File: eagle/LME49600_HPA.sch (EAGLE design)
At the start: 41 parts, among them IC1 OPA2134P, IC2 OPA2134P

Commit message: Update: Eagle files
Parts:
- C18, C19, C6, C7: value 4.7uF -> 10uF
- R11, R2, R3, R6, R7, R8: value 1.2k -> 1k
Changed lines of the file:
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@@
 <part name="AGND1" library="supply1" deviceset="AGND" device=""/>
 <part name="IC1" library="burr-brown" deviceset="OPA2134" device="P"/>
-<part name="R2" library="rcl" deviceset="R-EU_" device="0207/7" value="1.2k"/>
+<part name="R2" library="rcl" deviceset="R-EU_" device="0207/7" value="1k"/>
 <part name="AGND3" library="supply1" deviceset="AGND" device=""/>
 <part name="C2" library="rcl" deviceset="C-EU" device="025-024X044" value="0.1uF"/>
@@
 <part name="AGND4" library="supply1" deviceset="AGND" device=""/>
 <part name="AGND5" library="supply1" deviceset="AGND" device=""/>
-<part name="R3" library="rcl" deviceset="R-EU_" device="0207/7" value="1.2k"/>
+<part name="R3" library="rcl" deviceset="R-EU_" device="0207/7" value="1k"/>
 <part name="P+1" library="supply1" deviceset="V+" device=""/>
 <part name="P-1" library="supply1" deviceset="V-" device=""/>
@@
 <part name="AGND8" library="supply1" deviceset="AGND" device=""/>
 <part name="AGND9" library="supply1" deviceset="AGND" device=""/>
-<part name="R6" library="rcl" deviceset="R-EU_" device="0207/7" value="1.2k"/>
+<part name="R6" library="rcl" deviceset="R-EU_" device="0207/7" value="1k"/>
 <part name="AGND11" library="supply1" deviceset="AGND" device=""/>
 <part name="P+2" library="supply1" deviceset="V+" device=""/>
@@
 <part name="P-3" library="supply1" deviceset="V-" device=""/>
 <part name="FRAME1" library="frames" deviceset="A4P-LOC" device=""/>
-<part name="C6" library="rcl" deviceset="CPOL-EU" device="E2.5-5" value="4.7uF"/>
-<part name="C7" library="rcl" deviceset="CPOL-EU" device="E2.5-5" value="4.7uF"/>
+<part name="C6" library="rcl" deviceset="CPOL-EU" device="E2.5-5" value="10uF"/>
+<part name="C7" library="rcl" deviceset="CPOL-EU" device="E2.5-5" value="10uF"/>
 <part name="JP3" library="pinhead" deviceset="PINHD-1X2" device="" value="IN"/>
 <part name="AGND13" library="supply1" deviceset="AGND" device=""/>
 <part name="IC2" library="burr-brown" deviceset="OPA2134" device="P"/>
-<part name="R7" library="rcl" deviceset="R-EU_" device="0207/7" value="1.2k"/>
+<part name="R7" library="rcl" deviceset="R-EU_" device="0207/7" value="1k"/>
 <part name="AGND14" library="supply1" deviceset="AGND" device=""/>
 <part name="C12" library="rcl" deviceset="C-EU" device="025-024X044" value="0.1uF"/>
@@
 <part name="AGND15" library="supply1" deviceset="AGND" device=""/>
 <part name="AGND16" library="supply1" deviceset="AGND" device=""/>
-<part name="R8" library="rcl" deviceset="R-EU_" device="0207/7" value="1.2k"/>
+<part name="R8" library="rcl" deviceset="R-EU_" device="0207/7" value="1k"/>
 <part name="P+4" library="supply1" deviceset="V+" device=""/>
 <part name="P-4" library="supply1" deviceset="V-" device=""/>
@@
 <part name="AGND19" library="supply1" deviceset="AGND" device=""/>
 <part name="AGND20" library="supply1" deviceset="AGND" device=""/>
-<part name="R11" library="rcl" deviceset="R-EU_" device="0207/7" value="1.2k"/>
+<part name="R11" library="rcl" deviceset="R-EU_" device="0207/7" value="1k"/>
 <part name="P+5" library="supply1" deviceset="V+" device=""/>
 <part name="P-5" library="supply1" deviceset="V-" device=""/>
-<part name="C18" library="rcl" deviceset="CPOL-EU" device="E2.5-5" value="4.7uF"/>
-<part name="C19" library="rcl" deviceset="CPOL-EU" device="E2.5-5" value="4.7uF"/>
+<part name="C18" library="rcl" deviceset="CPOL-EU" device="E2.5-5" value="10uF"/>
+<part name="C19" library="rcl" deviceset="CPOL-EU" device="E2.5-5" value="10uF"/>
 <part name="U$1" library="mylib2" deviceset="LME49600-BRD3" device=""/>
 <part name="U$2" library="mylib2" deviceset="LME49600-BRD3" device=""/>

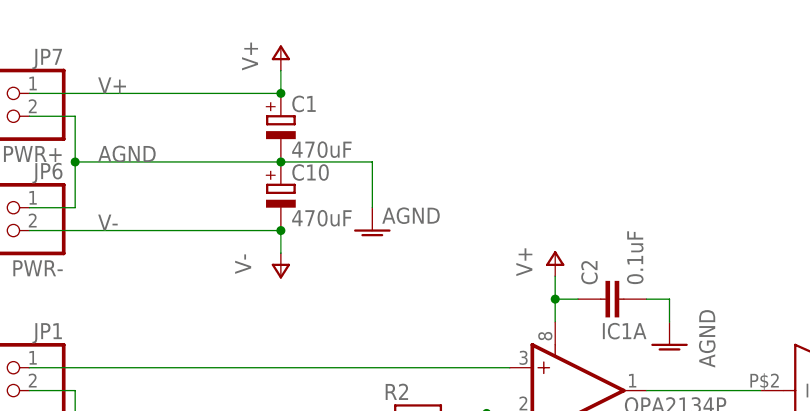
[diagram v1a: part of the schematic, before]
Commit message: Eagle Files: Add TP-GND
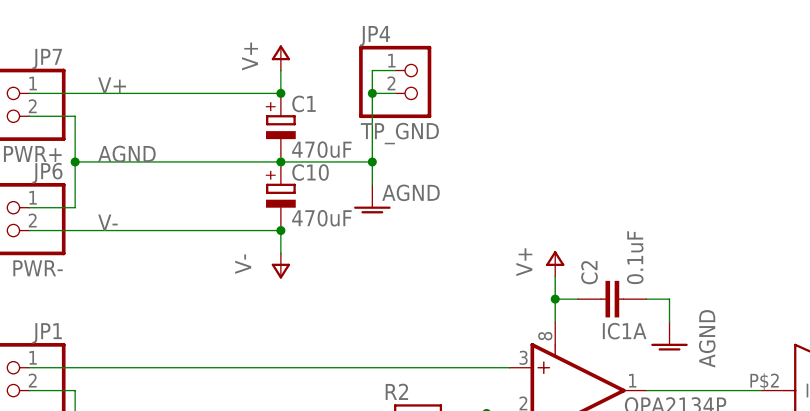
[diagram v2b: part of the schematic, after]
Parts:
- added JP4: TP_GND, pinhead:PINHD-1X2
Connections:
- net AGND: now also JP4.1, JP4.2
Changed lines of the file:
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@@
 <part name="JP6" library="pinhead" deviceset="PINHD-1X2" device="" value="PWR-"/>
 <part name="JP2" library="pinhead" deviceset="PINHD-1X3" device="" value="OUT"/>
+<part name="JP4" library="pinhead" deviceset="PINHD-1X2" device="" value="TP_GND"/>
 </parts>
 <sheets>
@@
 <instance part="C1" gate="G$1" x="60.96" y="218.44"/>
 <instance part="C10" gate="G$1" x="60.96" y="210.82"/>
-<instance part="AGND2" gate="VR1" x="71.12" y="205.74" smashed="yes">
-<attribute name="VALUE" x="78.74" y="208.28" size="1.778" layer="96" rot="R180"/>
+<instance part="AGND2" gate="VR1" x="71.12" y="208.28" smashed="yes">
+<attribute name="VALUE" x="78.74" y="210.82" size="1.778" layer="96" rot="R180"/>
 </instance>
 <instance part="P+3" gate="1" x="60.96" y="226.06"/>
@@
 <instance part="JP6" gate="G$1" x="30.48" y="205.74" rot="MR0"/>
 <instance part="JP2" gate="A" x="167.64" y="185.42"/>
+<instance part="JP4" gate="G$1" x="76.2" y="220.98"/>
 </instances>
 <busses>
@@
 <pinref part="AGND2" gate="VR1" pin="AGND"/>
 <wire x1="60.96" y1="213.36" x2="71.12" y2="213.36" width="0.1524" layer="91"/>
-<wire x1="71.12" y1="213.36" x2="71.12" y2="208.28" width="0.1524" layer="91"/>
+<wire x1="71.12" y1="213.36" x2="71.12" y2="210.82" width="0.1524" layer="91"/>
 <label x="40.64" y="213.36" size="1.778" layer="95"/>
 <pinref part="JP7" gate="G$1" pin="2"/>
@@
 <wire x1="38.1" y1="208.28" x2="38.1" y2="213.36" width="0.1524" layer="91"/>
 <junction x="38.1" y="213.36"/>
-</segment>
-<segment>
+<pinref part="JP4" gate="G$1" pin="1"/>
+<wire x1="73.66" y1="223.52" x2="71.12" y2="223.52" width="0.1524" layer="91"/>
+<wire x1="71.12" y1="223.52" x2="71.12" y2="220.98" width="0.1524" layer="91"/>
+<junction x="71.12" y="213.36"/>
+<pinref part="JP4" gate="G$1" pin="2"/>
+<wire x1="71.12" y1="220.98" x2="71.12" y2="213.36" width="0.1524" layer="91"/>
+<wire x1="73.66" y1="220.98" x2="71.12" y2="220.98" width="0.1524" layer="91"/>
+<junction x="71.12" y="220.98"/>
+</segment>
+<segment>

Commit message: Add: PWR LED
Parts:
- added JP5: PWR_LED, pinhead:PINHD-1X2
- added R1: 3.3k, rcl:R-EU_0207/7
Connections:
- new net N$16: JP5.2, R1.2
- net V+: now also JP5.1
- net V-: now also R1.1
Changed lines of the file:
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@@
 <setting verticaltext="up"/>
 </settings>
-<grid distance="0.1" unitdist="inch" unit="inch" style="lines" multiple="1" display="no" altdistance="0.01" altunitdist="inch" altunit="inch"/>
+<grid distance="0.1" unitdist="inch" unit="inch" style="dots" multiple="1" display="yes" altdistance="0.01" altunitdist="inch" altunit="inch"/>
 <layers>
-<layer number="1" name="Top" color="4" fill="1" visible="no" active="no"/>
-<layer number="16" name="Bottom" color="1" fill="1" visible="no" active="no"/>
-<layer number="17" name="Pads" color="2" fill="1" visible="no" active="no"/>
-<layer number="18" name="Vias" color="2" fill="1" visible="no" active="no"/>
-<layer number="19" name="Unrouted" color="6" fill="1" visible="no" active="no"/>
-<layer number="20" name="Dimension" color="15" fill="1" visible="no" active="no"/>
-<layer number="21" name="tPlace" color="7" fill="1" visible="no" active="no"/>
-<layer number="22" name="bPlace" color="7" fill="1" visible="no" active="no"/>
-<layer number="23" name="tOrigins" color="15" fill="1" visible="no" active="no"/>
-<layer number="24" name="bOrigins" color="15" fill="1" visible="no" active="no"/>
-<layer number="25" name="tNames" color="7" fill="1" visible="no" active="no"/>
-<layer number="26" name="bNames" color="7" fill="1" visible="no" active="no"/>
-<layer number="27" name="tValues" color="7" fill="1" visible="no" active="no"/>
-<layer number="28" name="bValues" color="7" fill="1" visible="no" active="no"/>
+<layer number="1" name="Top" color="4" fill="1" visible="yes" active="no"/>
+<layer number="16" name="Bottom" color="1" fill="1" visible="yes" active="no"/>
+<layer number="17" name="Pads" color="2" fill="1" visible="yes" active="no"/>
+<layer number="18" name="Vias" color="2" fill="1" visible="yes" active="no"/>
+<layer number="19" name="Unrouted" color="6" fill="1" visible="yes" active="no"/>
+<layer number="20" name="Dimension" color="15" fill="1" visible="yes" active="no"/>
+<layer number="21" name="tPlace" color="15" fill="1" visible="yes" active="no"/>
+<layer number="22" name="bPlace" color="15" fill="1" visible="yes" active="no"/>
+<layer number="23" name="tOrigins" color="15" fill="1" visible="yes" active="no"/>
+<layer number="24" name="bOrigins" color="15" fill="1" visible="yes" active="no"/>
+<layer number="25" name="tNames" color="7" fill="1" visible="yes" active="no"/>
+<layer number="26" name="bNames" color="7" fill="1" visible="yes" active="no"/>
+<layer number="27" name="tValues" color="7" fill="1" visible="yes" active="no"/>
+<layer number="28" name="bValues" color="7" fill="1" visible="yes" active="no"/>
 <layer number="29" name="tStop" color="7" fill="3" visible="no" active="no"/>
 <layer number="30" name="bStop" color="7" fill="6" visible="no" active="no"/>
@@
 <layer number="35" name="tGlue" color="7" fill="4" visible="no" active="no"/>
 <layer number="36" name="bGlue" color="7" fill="5" visible="no" active="no"/>
-<layer number="37" name="tTest" color="7" fill="1" visible="no" active="no"/>
-<layer number="38" name="bTest" color="7" fill="1" visible="no" active="no"/>
+<layer number="37" name="tTest" color="7" fill="1" visible="yes" active="no"/>
+<layer number="38" name="bTest" color="7" fill="1" visible="yes" active="no"/>
 <layer number="39" name="tKeepout" color="4" fill="11" visible="no" active="no"/>
 <layer number="40" name="bKeepout" color="1" fill="11" visible="no" active="no"/>
@@
 <layer number="44" name="Drills" color="7" fill="1" visible="no" active="no"/>
 <layer number="45" name="Holes" color="7" fill="1" visible="no" active="no"/>
-<layer number="46" name="Milling" color="3" fill="1" visible="no" active="no"/>
-<layer number="47" name="Measures" color="7" fill="1" visible="no" active="no"/>
-<layer number="48" name="Document" color="7" fill="1" visible="no" active="no"/>
-<layer number="49" name="Reference" color="7" fill="1" visible="no" active="no"/>
-<layer number="50" name="dxf" color="7" fill="1" visible="no" active="no"/>
-<layer number="51" name="tDocu" color="7" fill="1" visible="no" active="no"/>
-<layer number="52" name="bDocu" color="7" fill="1" visible="no" active="no"/>
+<layer number="46" name="Milling" color="3" fill="1" visible="yes" active="no"/>
+<layer number="47" name="Measures" color="7" fill="1" visible="yes" active="no"/>
+<layer number="48" name="Document" color="7" fill="1" visible="yes" active="no"/>
+<layer number="49" name="Reference" color="7" fill="1" visible="yes" active="no"/>
+<layer number="50" name="dxf" color="7" fill="1" visible="yes" active="no"/>
+<layer number="51" name="tDocu" color="7" fill="1" visible="yes" active="no"/>
+<layer number="52" name="bDocu" color="7" fill="1" visible="yes" active="no"/>
 <layer number="90" name="Modules" color="5" fill="1" visible="yes" active="yes"/>
 <layer number="91" name="Nets" color="2" fill="1" visible="yes" active="yes"/>
@@
 <part name="JP2" library="pinhead" deviceset="PINHD-1X3" device="" value="OUT"/>
 <part name="JP4" library="pinhead" deviceset="PINHD-1X2" device="" value="TP_GND"/>
+<part name="R1" library="rcl" deviceset="R-EU_" device="0207/7" value="3.3k"/>
+<part name="P+7" library="supply1" deviceset="V+" device=""/>
+<part name="P-7" library="supply1" deviceset="V-" device=""/>
+<part name="JP5" library="pinhead" deviceset="PINHD-1X2" device="" value="PWR_LED"/>
 </parts>
 <sheets>
@@
 <instance part="JP2" gate="A" x="167.64" y="185.42"/>
 <instance part="JP4" gate="G$1" x="76.2" y="220.98"/>
+<instance part="R1" gate="G$1" x="27.94" y="25.4" rot="R90"/>
+<instance part="P+7" gate="1" x="27.94" y="45.72"/>
+<instance part="P-7" gate="1" x="27.94" y="15.24"/>
+<instance part="JP5" gate="G$1" x="40.64" y="35.56"/>
 </instances>
 <busses>
@@
 <wire x1="38.1" y1="129.54" x2="38.1" y2="127" width="0.1524" layer="91"/>
 </segment>
+<segment>
+<pinref part="R1" gate="G$1" pin="1"/>
+<wire x1="27.94" y1="20.32" x2="27.94" y2="17.78" width="0.1524" layer="91"/>
+<pinref part="P-7" gate="1" pin="V-"/>
+</segment>
 </net>
 <net name="V+" class="0">
@@
 <pinref part="P+6" gate="1" pin="V+"/>
 <wire x1="25.4" y1="149.86" x2="25.4" y2="152.4" width="0.1524" layer="91"/>
+</segment>
+<segment>
+<pinref part="P+7" gate="1" pin="V+"/>
+<pinref part="JP5" gate="G$1" pin="1"/>
+<wire x1="38.1" y1="38.1" x2="27.94" y2="38.1" width="0.1524" layer="91"/>
+<wire x1="27.94" y1="38.1" x2="27.94" y2="43.18" width="0.1524" layer="91"/>
 </segment>
 </net>
@@
 </segment>
 </net>
+<net name="N$16" class="0">
+<segment>
+<pinref part="R1" gate="G$1" pin="2"/>
+<pinref part="JP5" gate="G$1" pin="2"/>
+<wire x1="38.1" y1="35.56" x2="27.94" y2="35.56" width="0.1524" layer="91"/>
+<wire x1="27.94" y1="35.56" x2="27.94" y2="30.48" width="0.1524" layer="91"/>
+</segment>
+</net>
